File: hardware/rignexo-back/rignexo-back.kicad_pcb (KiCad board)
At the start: 2 copper layers, 45 x 19.5 mm, 22 parts

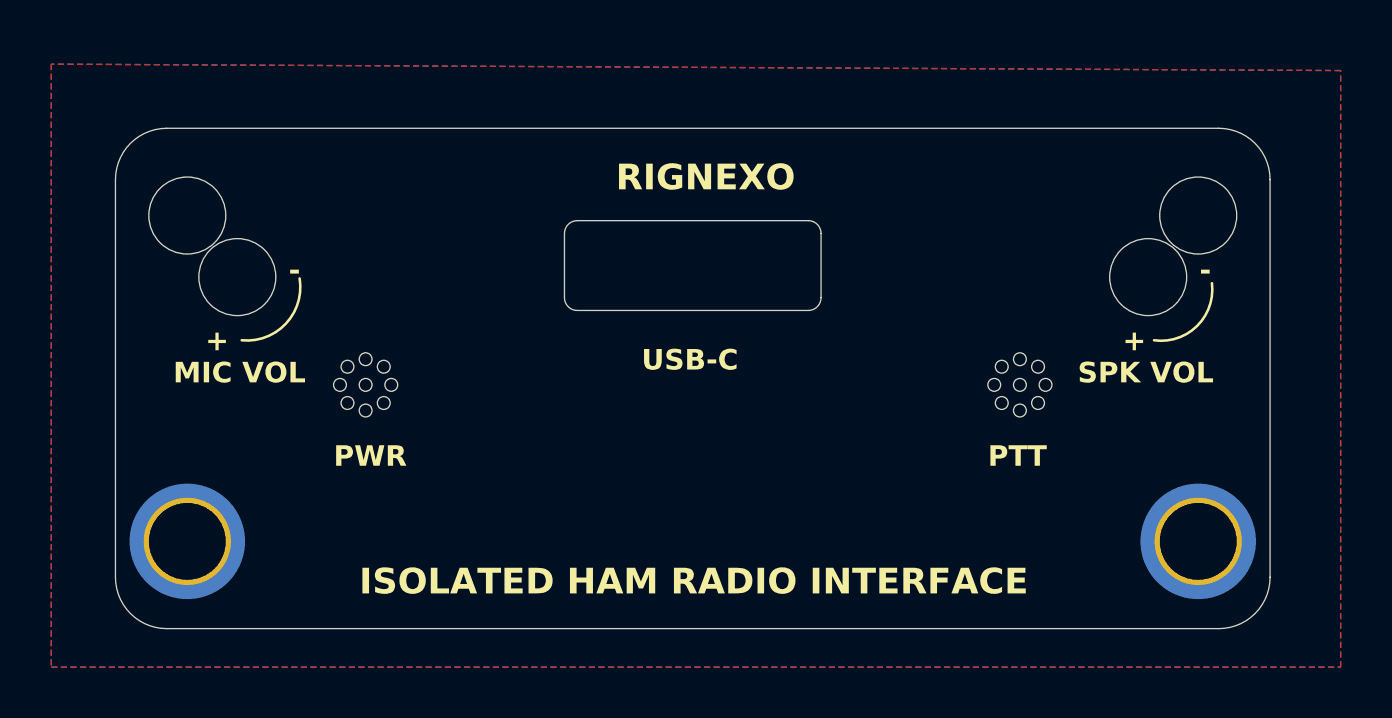
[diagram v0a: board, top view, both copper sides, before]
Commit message: Add single Gerbers after back-panel solder mask tweaks.
Slightly adjust the solder mask to improve electrical contact between the lid and the metal enclosure, then export updated single-board Gerbers.
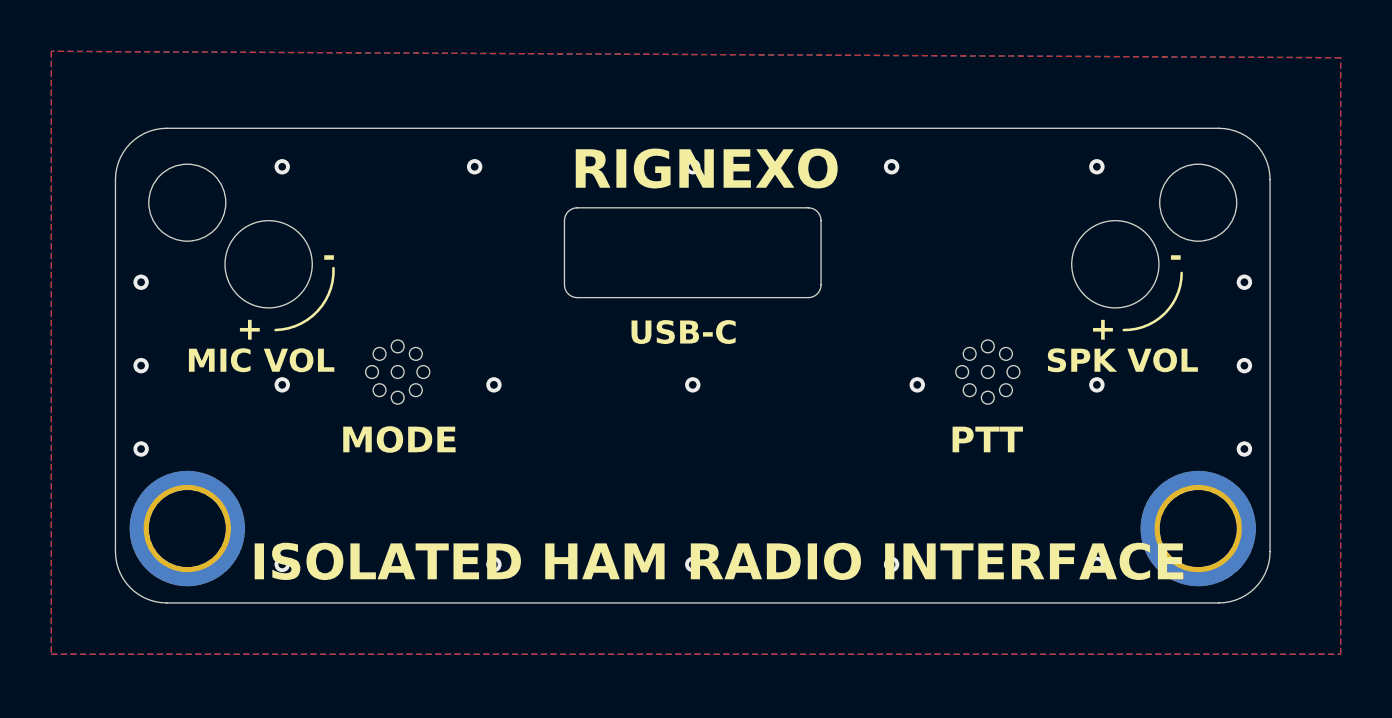
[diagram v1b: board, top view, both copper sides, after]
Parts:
- moved REF** 1.35 mm to (135.0, 109.5)
- moved REF** 1.35 mm to (111.7, 108.8)
- moved REF** 1.35 mm to (134.0, 110.5)
- moved REF** 1.35 mm to (133.3, 110.2)
- moved REF** 1.35 mm to (111.0, 109.5)
- moved REF** 1.35 mm to (110.3, 110.2)
- moved REF** 1.35 mm to (110.0, 109.5)
- moved REF** 1.35 mm to (111.7, 110.2)
- moved REF** 1.35 mm to (111.0, 108.5)
- moved REF** 1.35 mm to (112.0, 109.5)
- moved REF** 1.35 mm to (134.0, 109.5)
- moved REF** 1.35 mm to (134.7, 110.2)
- moved REF** 1.35 mm to (134.0, 108.5)
- moved REF** 1.35 mm to (133.3, 108.8)
- moved REF** 1.35 mm to (134.7, 108.8)
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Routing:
- net GND: vias 0 -> 21
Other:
- board size 45 x 19.5 mm -> 45 x 19 mm
- board text added: "MODE"
- board text removed: "PWR"
